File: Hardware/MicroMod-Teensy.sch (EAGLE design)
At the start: 71 parts, among them J1 MICROMOD-2222, Q1 20V/4.2A/52mΩ/1.4W, Q2 20V/0.2A/8MHz/1.2Ω/1Vth, U1 IMXRT1062DV10X10, U3 MKL02Z32VFG4, U4 W25QXX128MBIT-6X5, Y1 32.768kHz, Y2 24MHz

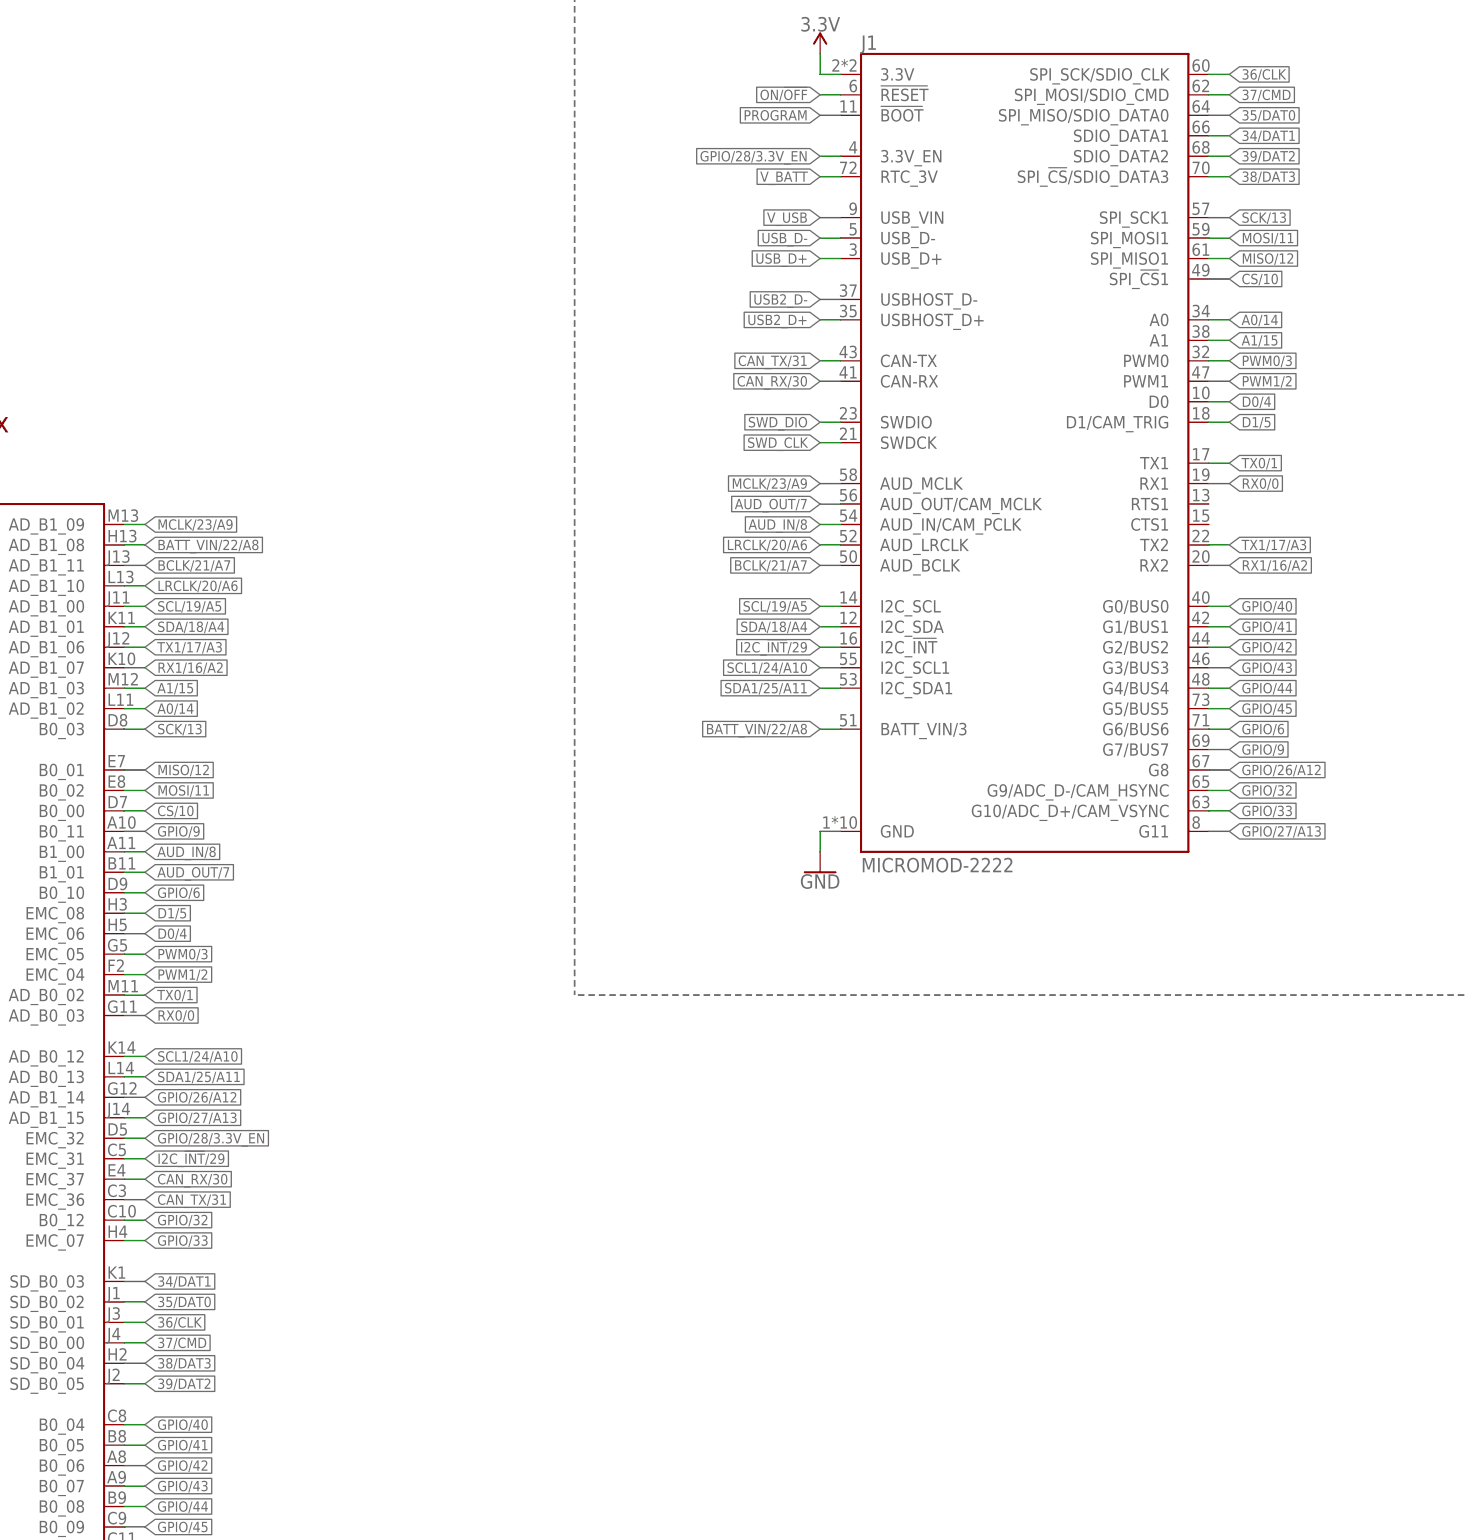
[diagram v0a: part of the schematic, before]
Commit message: Fix DAT2/DAT3, now correctly connected to B0_04 and B0_05.
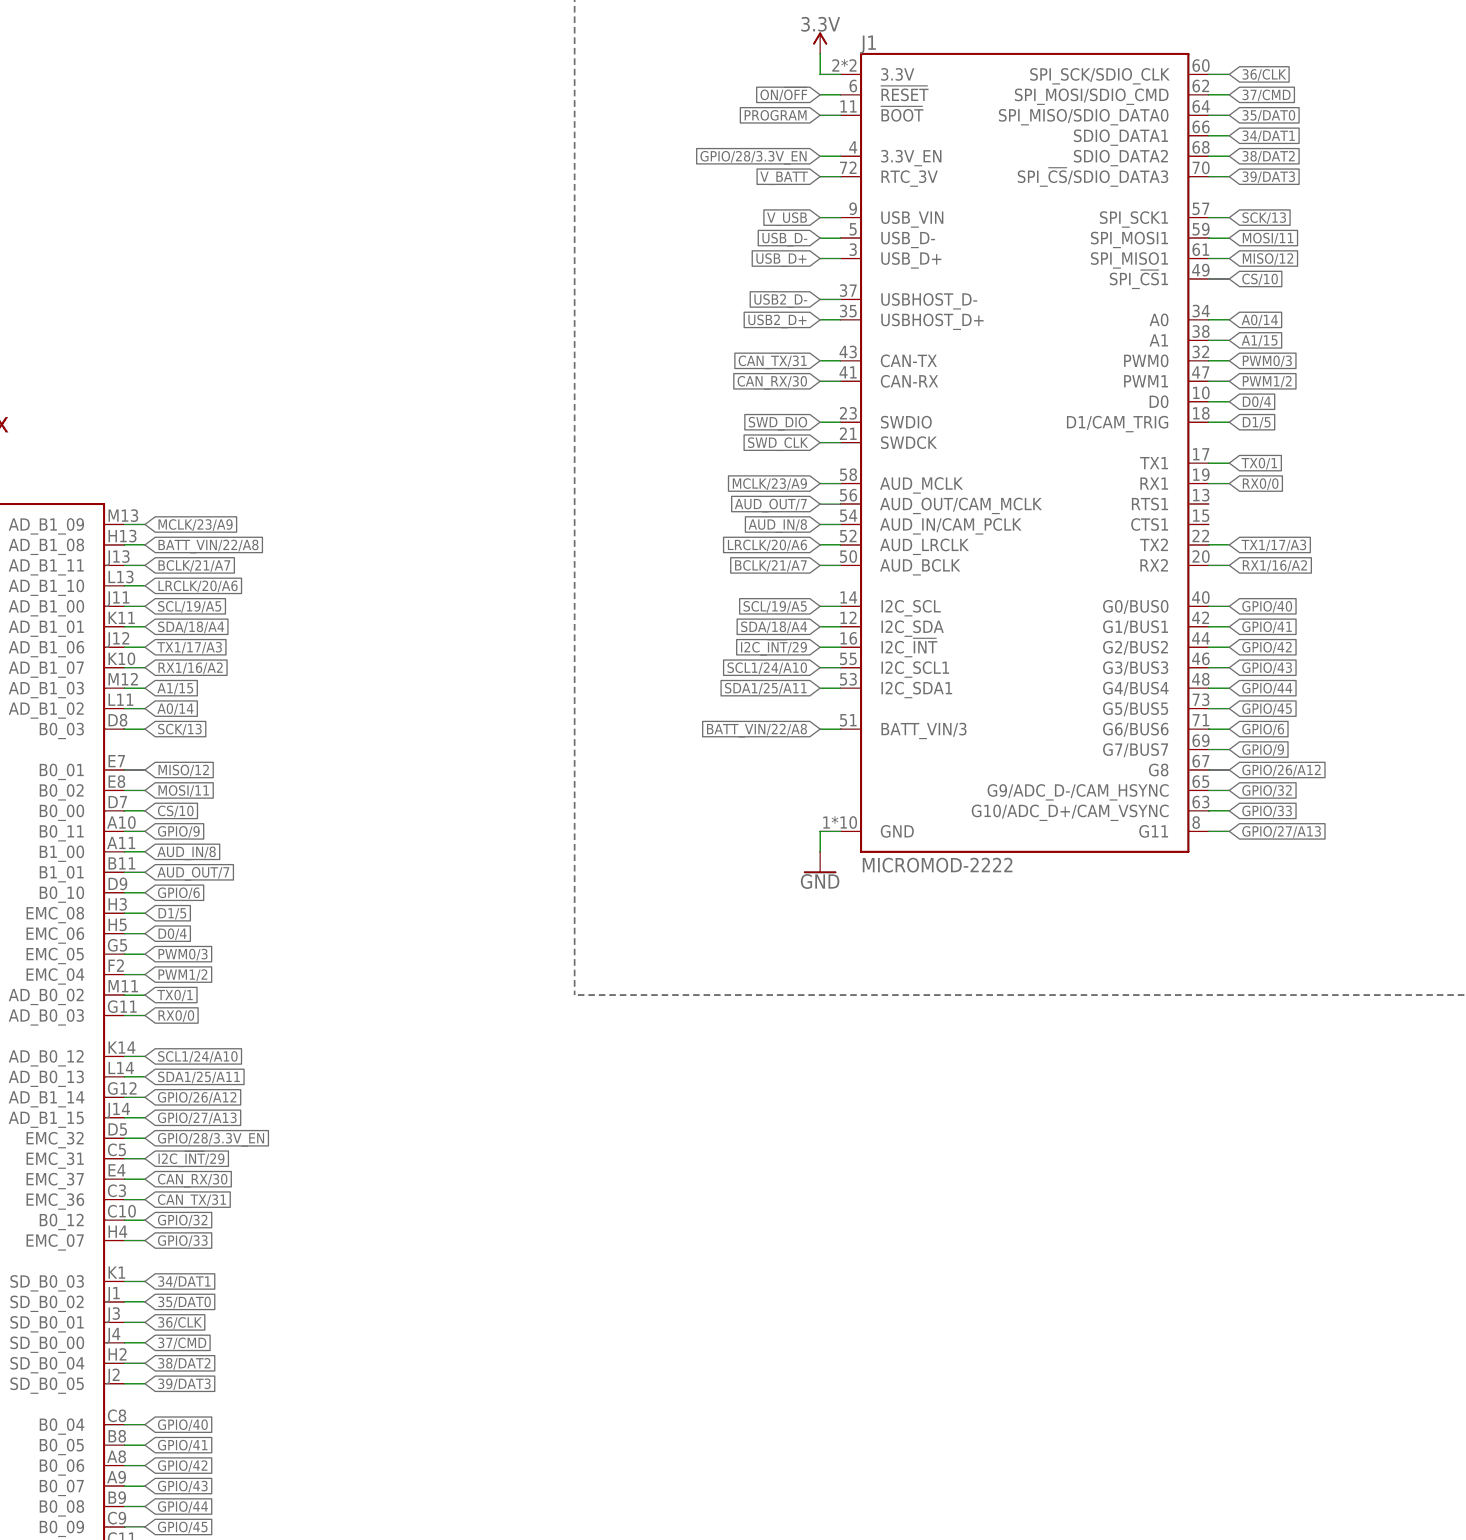
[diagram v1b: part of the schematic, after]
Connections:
- removed net 38/DAT3: J1.SPI_!CS!/SDIO_DATA3, U1.SD_B0_04
- removed net 39/DAT2: J1.SDIO_DATA2, U1.SD_B0_05
- new net 38/DAT2: J1.SDIO_DATA2, U1.SD_B0_04
- new net 39/DAT3: J1.SPI_!CS!/SDIO_DATA3, U1.SD_B0_05
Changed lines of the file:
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@@
 <?xml version="1.0" encoding="utf-8"?>
 <!DOCTYPE eagle SYSTEM "eagle.dtd">
-<eagle version="9.6.0">
+<eagle version="9.6.2">
 <drawing>
 <settings>
@@
 </segment>
 </net>
-<net name="38/DAT3" class="0">
-<segment>
-<wire x1="162.56" y1="93.98" x2="165.1" y2="93.98" width="0.1524" layer="91"/>
-<pinref part="U1" gate="U1" pin="SD_B0_04"/>
-<label x="165.1" y="93.98" size="1.27" layer="95" xref="yes"/>
-</segment>
+<net name="39/DAT3" class="0">
 <segment>
 <wire x1="297.18" y1="241.3" x2="299.72" y2="241.3" width="0.1524" layer="91"/>
@@
 <pinref part="J1" gate="J1" pin="SPI_!CS!/SDIO_DATA3"/>
 </segment>
-</net>
-<net name="39/DAT2" class="0">
 <segment>
 <wire x1="162.56" y1="91.44" x2="165.1" y2="91.44" width="0.1524" layer="91"/>
 <pinref part="U1" gate="U1" pin="SD_B0_05"/>
 <label x="165.1" y="91.44" size="1.27" layer="95" xref="yes"/>
-</segment>
-<segment>
-<wire x1="297.18" y1="243.84" x2="299.72" y2="243.84" width="0.1524" layer="91"/>
-<label x="299.72" y="243.84" size="1.27" layer="95" xref="yes"/>
-<pinref part="J1" gate="J1" pin="SDIO_DATA2"/>
 </segment>
 </net>
@@
 </segment>
 </net>
+<net name="38/DAT2" class="0">
+<segment>
+<wire x1="162.56" y1="93.98" x2="165.1" y2="93.98" width="0.1524" layer="91"/>
+<pinref part="U1" gate="U1" pin="SD_B0_04"/>
+<label x="165.1" y="93.98" size="1.27" layer="95" xref="yes"/>
+</segment>
+<segment>
+<wire x1="297.18" y1="243.84" x2="299.72" y2="243.84" width="0.1524" layer="91"/>
+<label x="299.72" y="243.84" size="1.27" layer="95" xref="yes"/>
+<pinref part="J1" gate="J1" pin="SDIO_DATA2"/>
+</segment>
+</net>

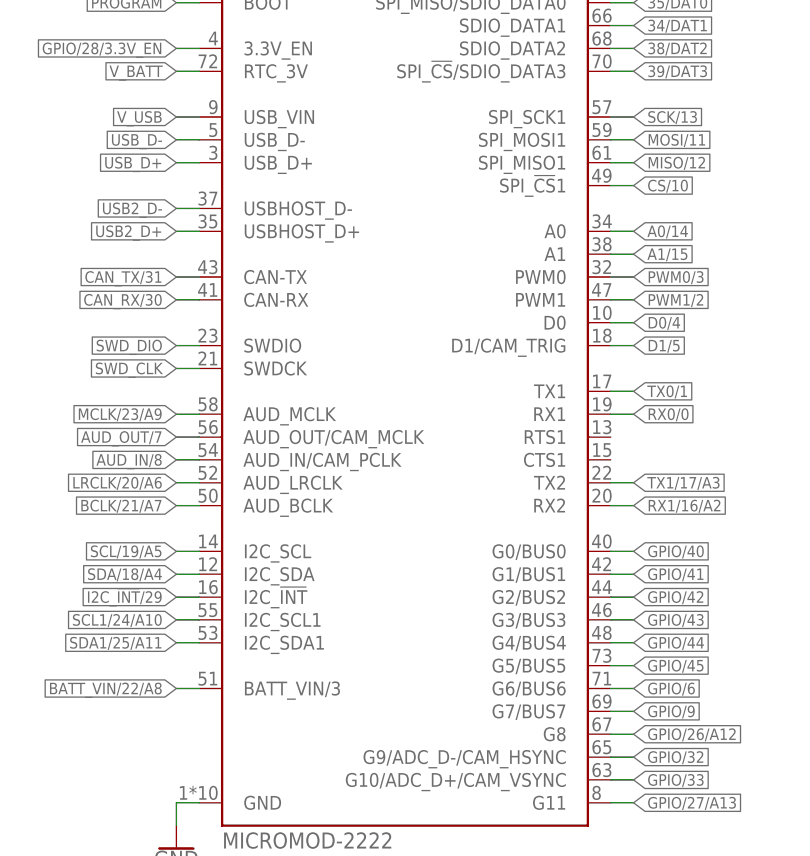
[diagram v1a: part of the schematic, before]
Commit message: Fix incorrect SDA/SCL1 board edge connector pinout
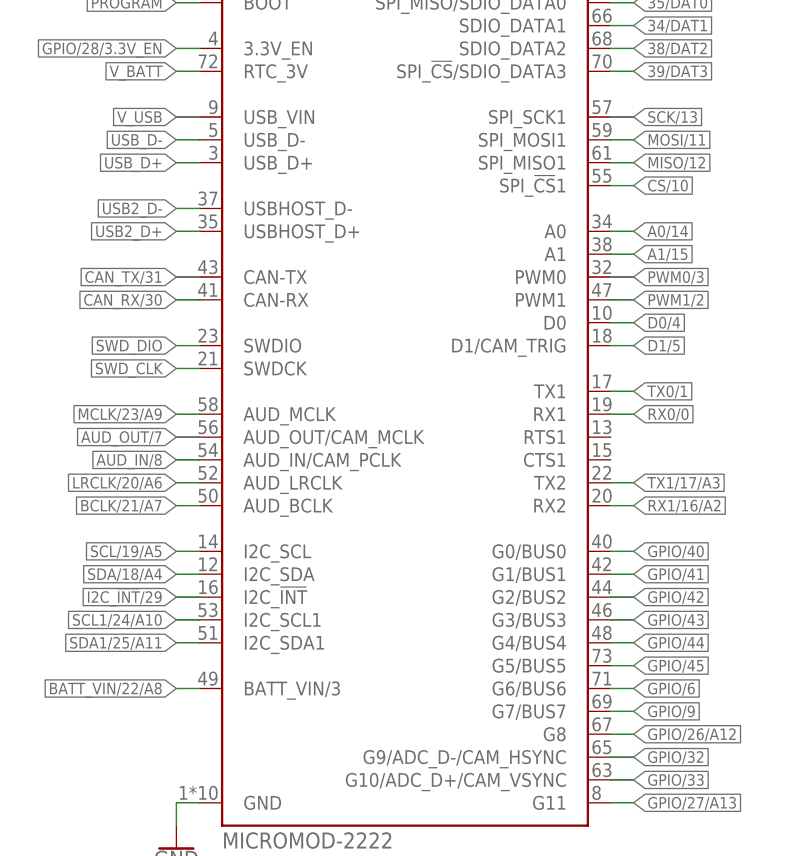
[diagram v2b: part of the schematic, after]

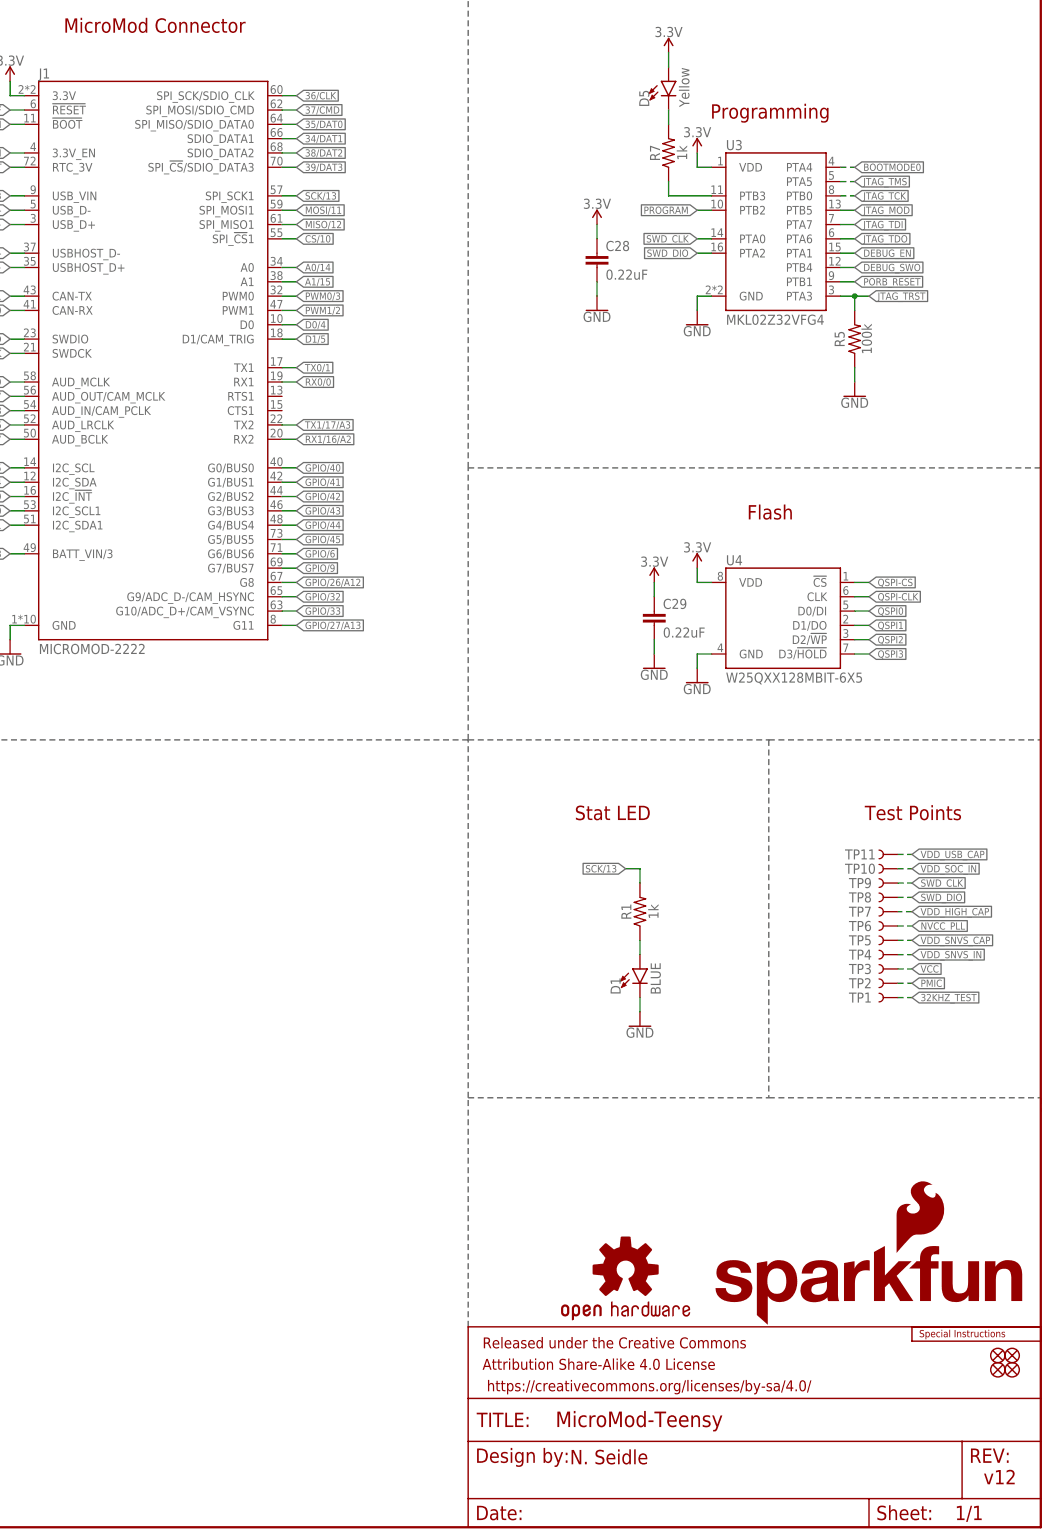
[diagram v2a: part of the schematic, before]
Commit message: Update copper to v13. Add production files.
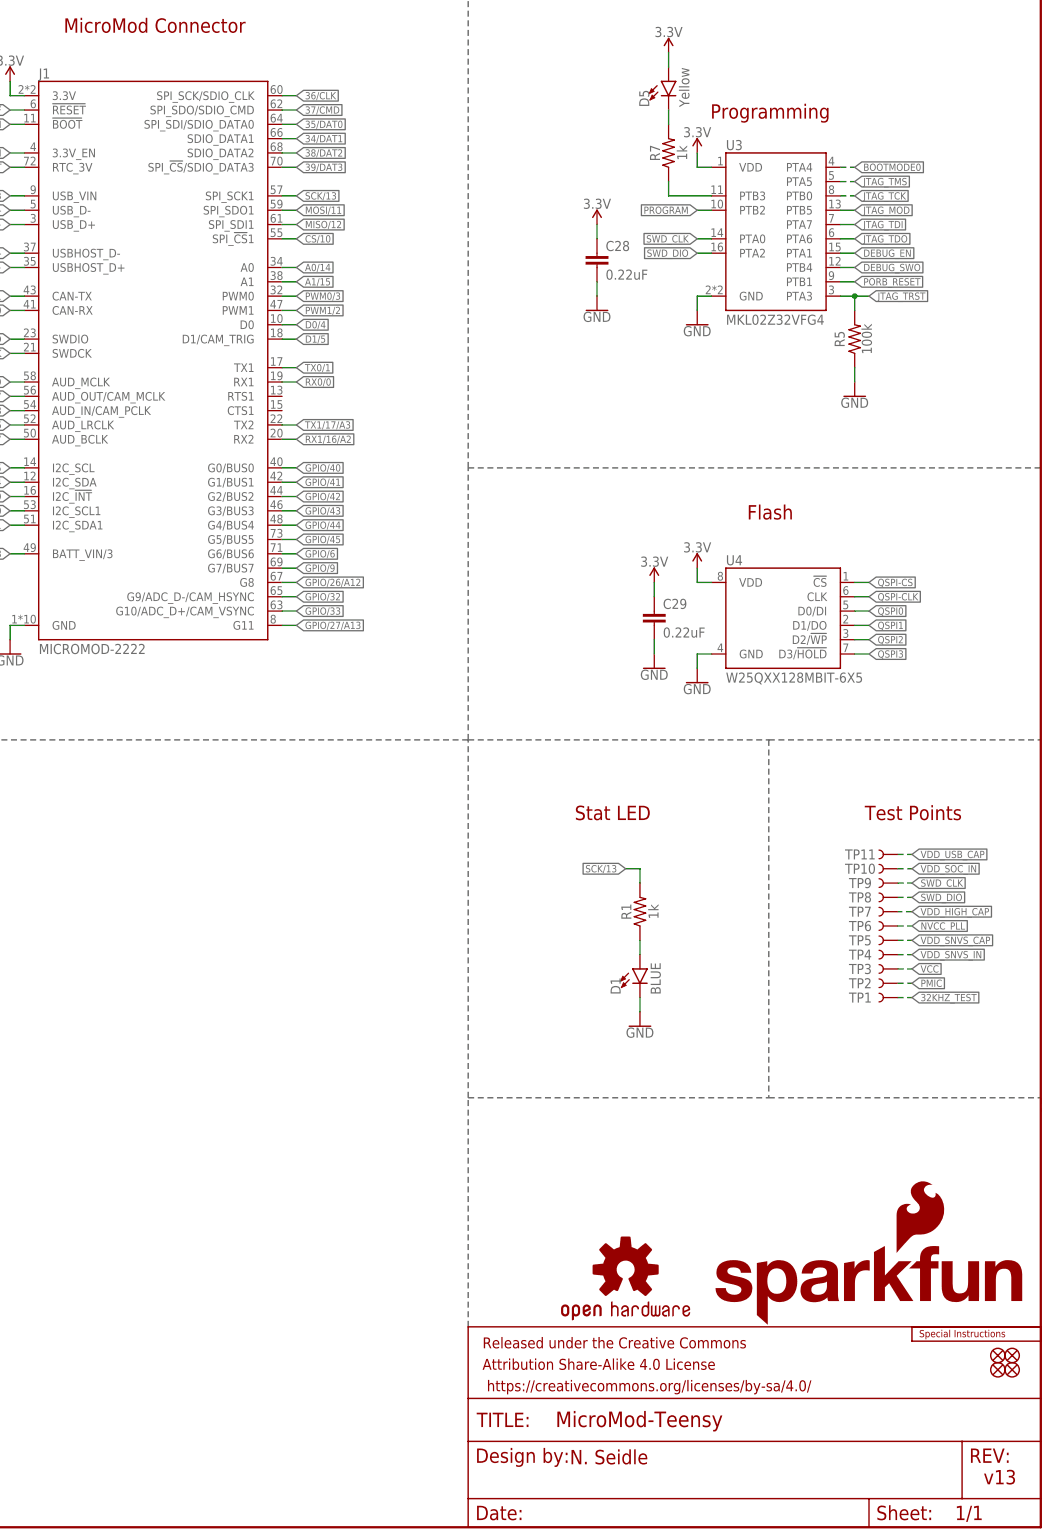
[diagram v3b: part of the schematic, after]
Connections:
- net 35/DAT0: now also J1.SPI_SDI/SDIO_DATA0; no longer J1.SPI_MISO/SDIO_DATA0
- net 37/CMD: now also J1.SPI_SDO/SDIO_CMD; no longer J1.SPI_MOSI/SDIO_CMD
- net MISO/12: now also J1.SPI_SDI1; no longer J1.SPI_MISO1
- net MOSI/11: now also J1.SPI_SDO1; no longer J1.SPI_MOSI1
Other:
- note added: "v13"
- note removed: "v12"
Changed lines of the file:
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@@
 <?xml version="1.0" encoding="utf-8"?>
 <!DOCTYPE eagle SYSTEM "eagle.dtd">
-<eagle version="9.6.2">
+<eagle version="9.6.0">
 <drawing>
 <settings>
@@
 <sheet>
 <plain>
-<text x="421.64" y="7.62" size="2.54" layer="94">v12</text>
+<text x="421.64" y="7.62" size="2.54" layer="94">v13</text>
 <text x="348.234" y="11.176" size="2.54" layer="94">N. Seidle</text>
 <text x="274.574" y="266.446" size="2.54" layer="94" font="vector" align="center">MicroMod Connector</text>
@@
 <wire x1="297.18" y1="231.14" x2="299.72" y2="231.14" width="0.1524" layer="91"/>
 <label x="299.72" y="231.14" size="1.27" layer="95" rot="MR180" xref="yes"/>
-<pinref part="J1" gate="J1" pin="SPI_MISO1"/>
+<pinref part="J1" gate="J1" pin="SPI_SDI1"/>
 </segment>
 </net>
@@
 <wire x1="297.18" y1="233.68" x2="299.72" y2="233.68" width="0.1524" layer="91"/>
 <label x="299.72" y="233.68" size="1.27" layer="95" rot="MR180" xref="yes"/>
-<pinref part="J1" gate="J1" pin="SPI_MOSI1"/>
+<pinref part="J1" gate="J1" pin="SPI_SDO1"/>
 </segment>
 </net>
@@
 <wire x1="297.18" y1="248.92" x2="299.72" y2="248.92" width="0.1524" layer="91"/>
 <label x="299.72" y="248.92" size="1.27" layer="95" xref="yes"/>
-<pinref part="J1" gate="J1" pin="SPI_MISO/SDIO_DATA0"/>
+<pinref part="J1" gate="J1" pin="SPI_SDI/SDIO_DATA0"/>
 </segment>
 </net>
@@
 <wire x1="297.18" y1="251.46" x2="299.72" y2="251.46" width="0.1524" layer="91"/>
 <label x="299.72" y="251.46" size="1.27" layer="95" xref="yes"/>
-<pinref part="J1" gate="J1" pin="SPI_MOSI/SDIO_CMD"/>
-</segment>
-</net>
+<pinref part="J1" gate="J1" pin="SPI_SDO/SDIO_CMD"/>
+</segment>
+</net>
